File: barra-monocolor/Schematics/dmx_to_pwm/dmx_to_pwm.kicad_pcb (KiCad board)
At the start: 2 copper layers, 46 x 162.3 mm, 50 parts, among them J1 RJ45, J2 RJ45, J3 Conn_02x04_Top_Bottom, J5 Conn_01x05_Socket, Q1 TIP41, Q2 TIP41, Q3 TIP41, Q5 TIP41, SW1 SW_DIP_x08, U2 LM2596T-5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

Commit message: updated max patches
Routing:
- net 5V: track 224.1 -> 219.0 mm
- net Net-(D3-A): track 62.6 -> 62.1 mm

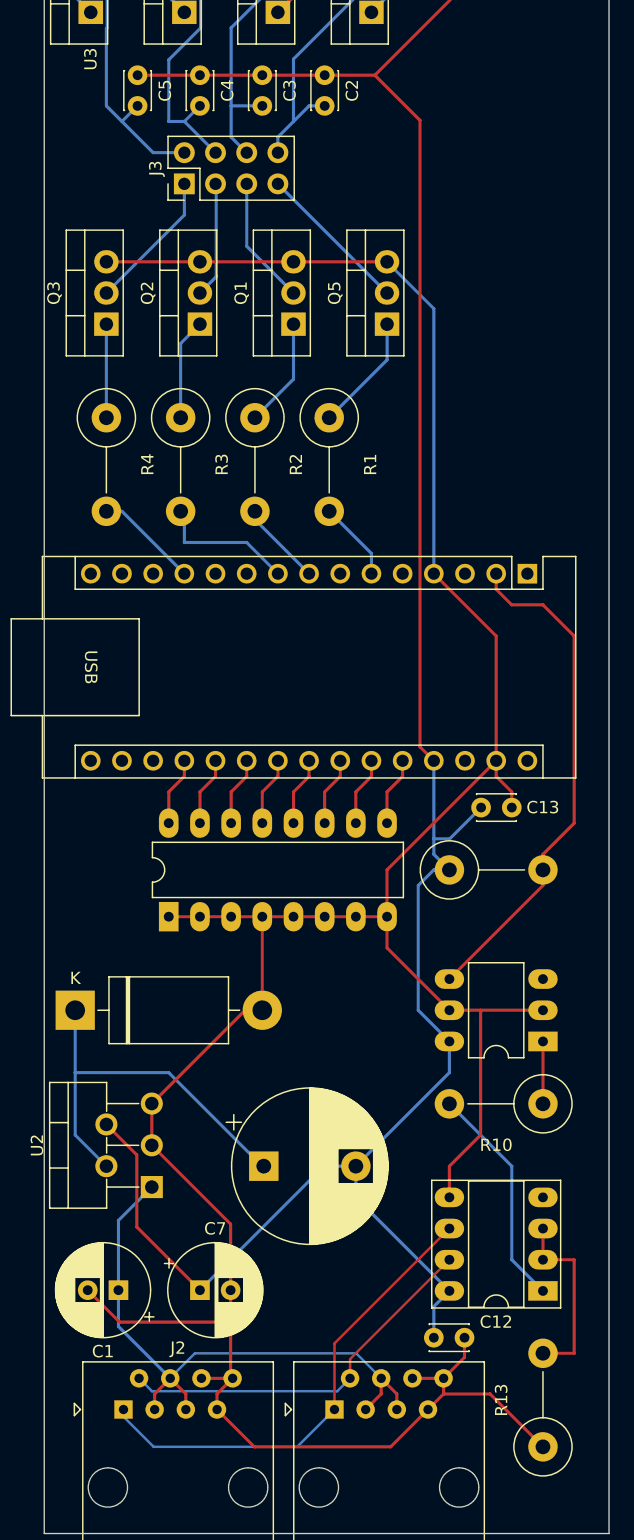
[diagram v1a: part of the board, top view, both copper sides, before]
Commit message: improved pcb track width, added antenna connector
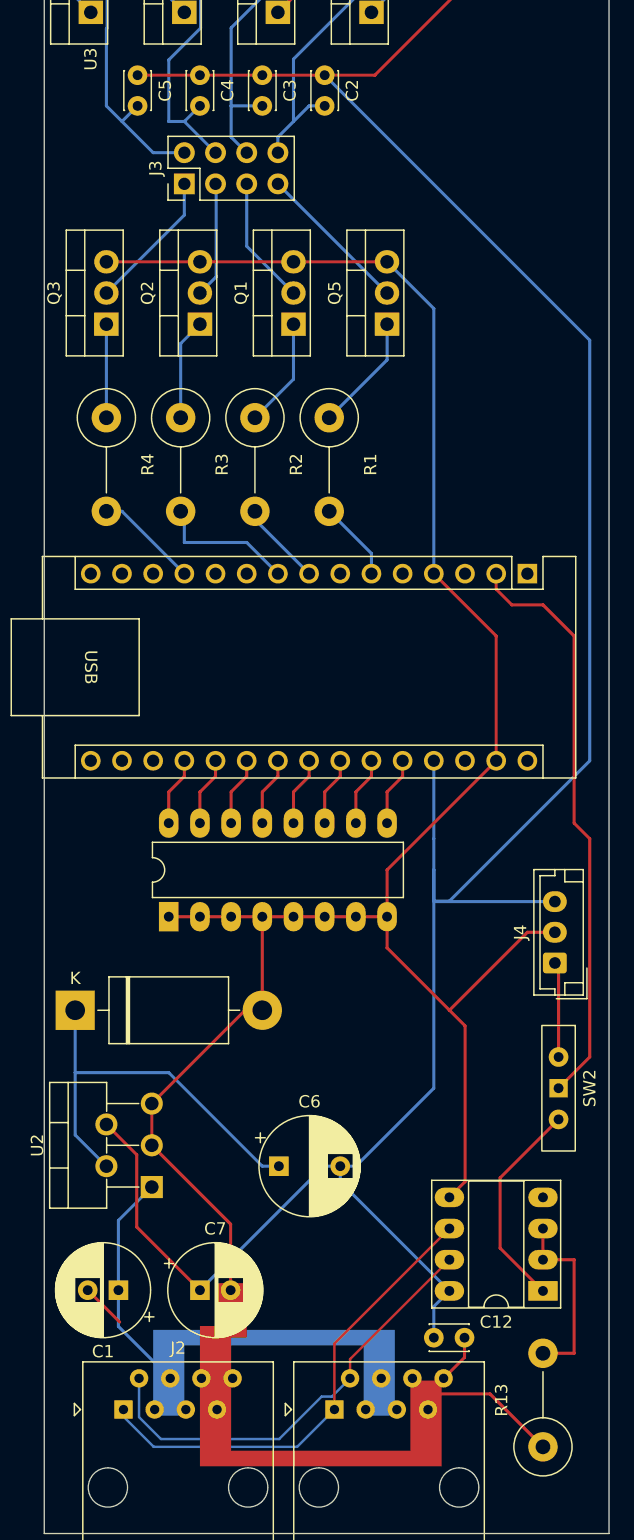
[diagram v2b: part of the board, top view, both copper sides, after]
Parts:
- removed C13: 100nF, Capacitor_THT:C_Disc_D3.0mm_W2.0mm_P2.50mm
- removed L1: 100uH, Capacitor_THT:CP_Radial_D12.5mm_P7.50mm
- removed R10: 470, Resistor_THT:R_Axial_DIN0414_L11.9mm_D4.5mm_P7.62mm_Vertical
- removed R14: 1K, Resistor_THT:R_Axial_DIN0414_L11.9mm_D4.5mm_P7.62mm_Vertical
- removed U9: H11L1, Package_DIP:DIP-6_W7.62mm_LongPads
- added C6: 33uH, Capacitor_THT:CP_Radial_D8.0mm_P5.00mm, F.Cu at (86.4, 154.9)
- added J4: Conn_01x03_Socket, Connector_JST:JST_EH_B3B-EH-A_1x03_P2.50mm_Vertical, F.Cu at (108.9, 138.4)
- added SW2: SW_Wuerth, Button_Switch_THT:SW_Slide-03_Wuerth-WS-SLTV_10x2.5x6.4_P2.54mm, F.Cu at (109.2, 148.6)
- C1: value 47uF - 50V -> 47uF - 100V
- C7: value 47uF - 50V -> 47uF - 16V
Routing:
- net GND: track 241.7 -> 203.6 mm
- net VCC: track 49.6 -> 18.5 mm
- net 5V: track 219.0 -> 247.5 mm
- net Net-(J4-Pin_1): track 0.00 -> 7.78 mm
- net Net-(A1-D0/RX): track 41.3 -> 47.6 mm
- net Net-(R10-Pad1): track 5.08 -> 0.00 mm
- net DATA-: track 31.1 -> 36.1 mm
- net Net-(D2-K): track 32.3 -> 33.5 mm
- net Net-(SW2-A): track 18.4 -> 17.4 mm

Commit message: stuff
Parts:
- removed D5: 1N4004, Diode_THT:D_DO-41_SOD81_P7.62mm_Horizontal
- removed U6: LM337_TO220, Package_TO_SOT_THT:TO-220-3_Vertical
- added D1: 1N4004, Diode_THT:D_DO-41_SOD81_P7.62mm_Horizontal, F.Cu at (96.5, 35.6)
- added H1: MountingHole_Pad, MountingHole:MountingHole_3.2mm_M3_Pad, F.Cu at (109.2, 47.6)
- added H2: MountingHole_Pad, MountingHole:MountingHole_3.2mm_M3_Pad, F.Cu at (71.8, 74.3)
- added H3: MountingHole_Pad, MountingHole:MountingHole_3.2mm_M3_Pad, F.Cu at (71.8, 130.8)
- added H4: MountingHole_Pad, MountingHole:MountingHole_3.2mm_M3_Pad, F.Cu at (96.5, 148.0)
- added H5: MountingHole_Pad, MountingHole:MountingHole_3.2mm_M3_Pad, F.Cu at (104.8, 94.0)
- added U1: LM317_TO-220, Package_TO_SOT_THT:TO-220-3_Vertical, F.Cu at (70.2, 56.5)
- U3, U4, U5: value LM337_TO220 -> LM317_TO-220
- moved D4 11.2 mm to (96.5, 51.4), turned to 0 degrees
- moved D3 10.8 mm to (96.5, 43.2), turned to 0 degrees
- moved U4 8.28 mm to (85.7, 56.5), turned to -90 degrees
- moved U3 7.75 mm to (77.5, 56.5), turned to -90 degrees
- moved D6 7.62 mm to (96.5, 27.9), turned to 0 degrees
- moved U5 4.45 mm to (94.0, 56.5), turned to -90 degrees
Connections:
- C10 pad 1: 5V -> GND
- C10 pad 2: Net-(D5-A) -> Net-(D1-K)
- C11 pad 1: 5V -> GND
- C11 pad 2: Net-(D6-A) -> Net-(D6-K)
- C2 pad 1: 5V -> GND
- C3 pad 1: 5V -> GND
- C4 pad 1: 5V -> GND
- C5 pad 1: 5V -> GND
- C8 pad 1: 5V -> GND
- C8 pad 2: Net-(D3-A) -> Net-(D4-K)
- C9 pad 1: 5V -> GND
- C9 pad 2: Net-(D4-A) -> Net-(D3-K)
- D3 pad 1: 5V -> Net-(D3-K)
- D3 pad 2: Net-(D3-A) -> GND
- D4 pad 1: 5V -> Net-(D4-K)
- D4 pad 2: Net-(D4-A) -> GND
- D6 pad 1: 5V -> Net-(D6-K)
- D6 pad 2: Net-(D6-A) -> GND
- J5 pad 1: Net-(D3-A) -> Net-(D4-K)
- J5 pad 2: Net-(D4-A) -> Net-(D3-K)
- J5 pad 3: 5V -> GND
- J5 pad 4: Net-(D5-A) -> Net-(D1-K)
- J5 pad 5: Net-(D6-A) -> Net-(D6-K)
- Q1 pad 2: L2-SOC-IN -> 5V
- Q1 pad 3: GND -> L2-SOC-IN
- Q2 pad 2: L3-SOC-IN -> 5V
- Q2 pad 3: GND -> L3-SOC-IN
- Q3 pad 2: L4-SOC-IN -> 5V
- Q3 pad 3: GND -> L4-SOC-IN
- Q5 pad 2: L1-SOC-IN -> 5V
- Q5 pad 3: GND -> L1-SOC-IN
- R7 pad 2: Net-(U6-VO) -> Net-(U4-VO)
- R8 pad 2: Net-(U4-VO) -> Net-(U3-VO)
- R9 pad 2: Net-(U3-VO) -> Net-(U1-VO)
- RV1 pad 3: Net-(D3-A) -> Net-(D4-K)
- RV2 pad 3: Net-(D4-A) -> Net-(D3-K)
- RV3 pad 3: Net-(D5-A) -> Net-(D1-K)
- RV4 pad 3: Net-(D6-A) -> Net-(D6-K)
- U3 pad 1: Net-(D6-A) -> Net-(D1-K)
- U3 pad 2: L4-SOC-OUT -> Net-(U3-VO)
- U3 pad 3: Net-(U3-VO) -> L3-SOC-OUT
- U4 pad 1: Net-(D5-A) -> Net-(D3-K)
- U4 pad 2: L3-SOC-OUT -> Net-(U4-VO)
- U4 pad 3: Net-(U4-VO) -> L2-SOC-OUT
- U5 pad 1: Net-(D3-A) -> Net-(D4-K)
- U5 pad 2: L1-SOC-OUT -> Net-(U5-VO)
- U5 pad 3: Net-(U5-VO) -> L1-SOC-OUT
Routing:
- net Net-(D6-A): track 80.6 -> 0.00 mm
- net GND: track 203.6 -> 283.9 mm
- net Net-(D6-K): track 0.00 -> 77.6 mm
- net Net-(D5-A): track 76.8 -> 0.00 mm
- net Net-(D4-A): track 73.5 -> 0.00 mm
- net Net-(D1-K): track 0.00 -> 73.3 mm
- net Net-(D3-K): track 0.00 -> 67.4 mm
- net Net-(D3-A): track 62.1 -> 0.00 mm
- net Net-(D4-K): track 0.00 -> 55.9 mm
- net 5V: track 247.5 -> 194.7 mm
- net VCC: track 18.5 -> 0.00 mm
- net Net-(U1-VO): track 0.00 -> 11.9 mm
- net Net-(U3-VO): track 5.08 -> 11.8 mm
- net Net-(U6-VO): track 6.13 -> 0.00 mm
- net L3-SOC-OUT: track 19.7 -> 14.9 mm
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
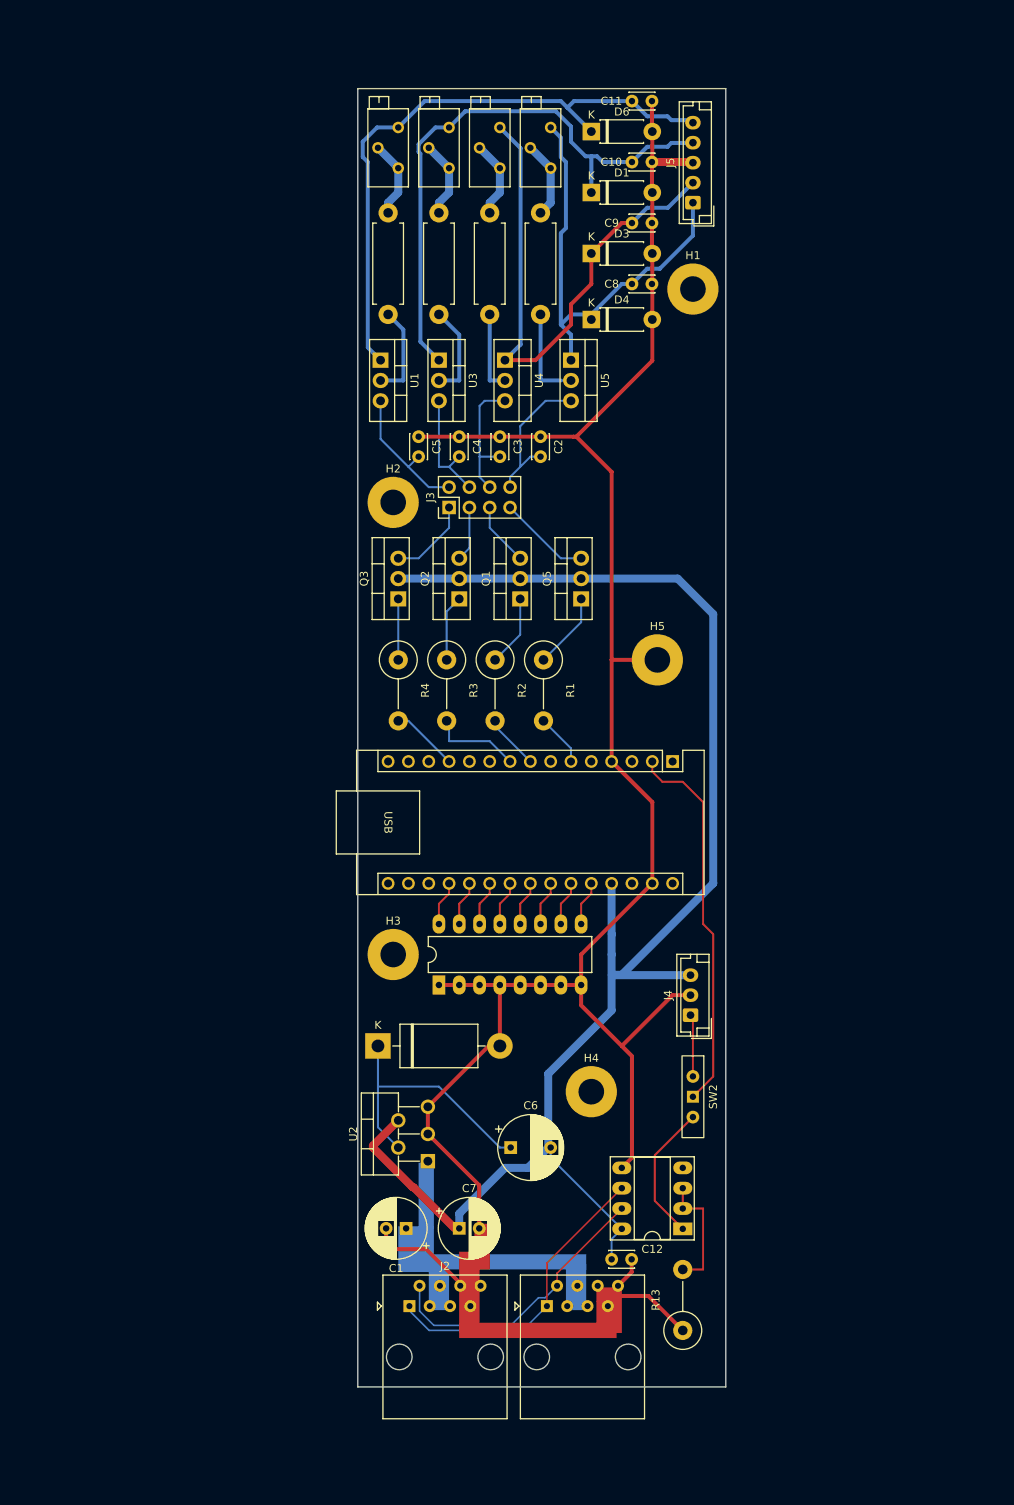
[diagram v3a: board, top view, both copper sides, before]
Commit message: updated schematics to 6 lasers
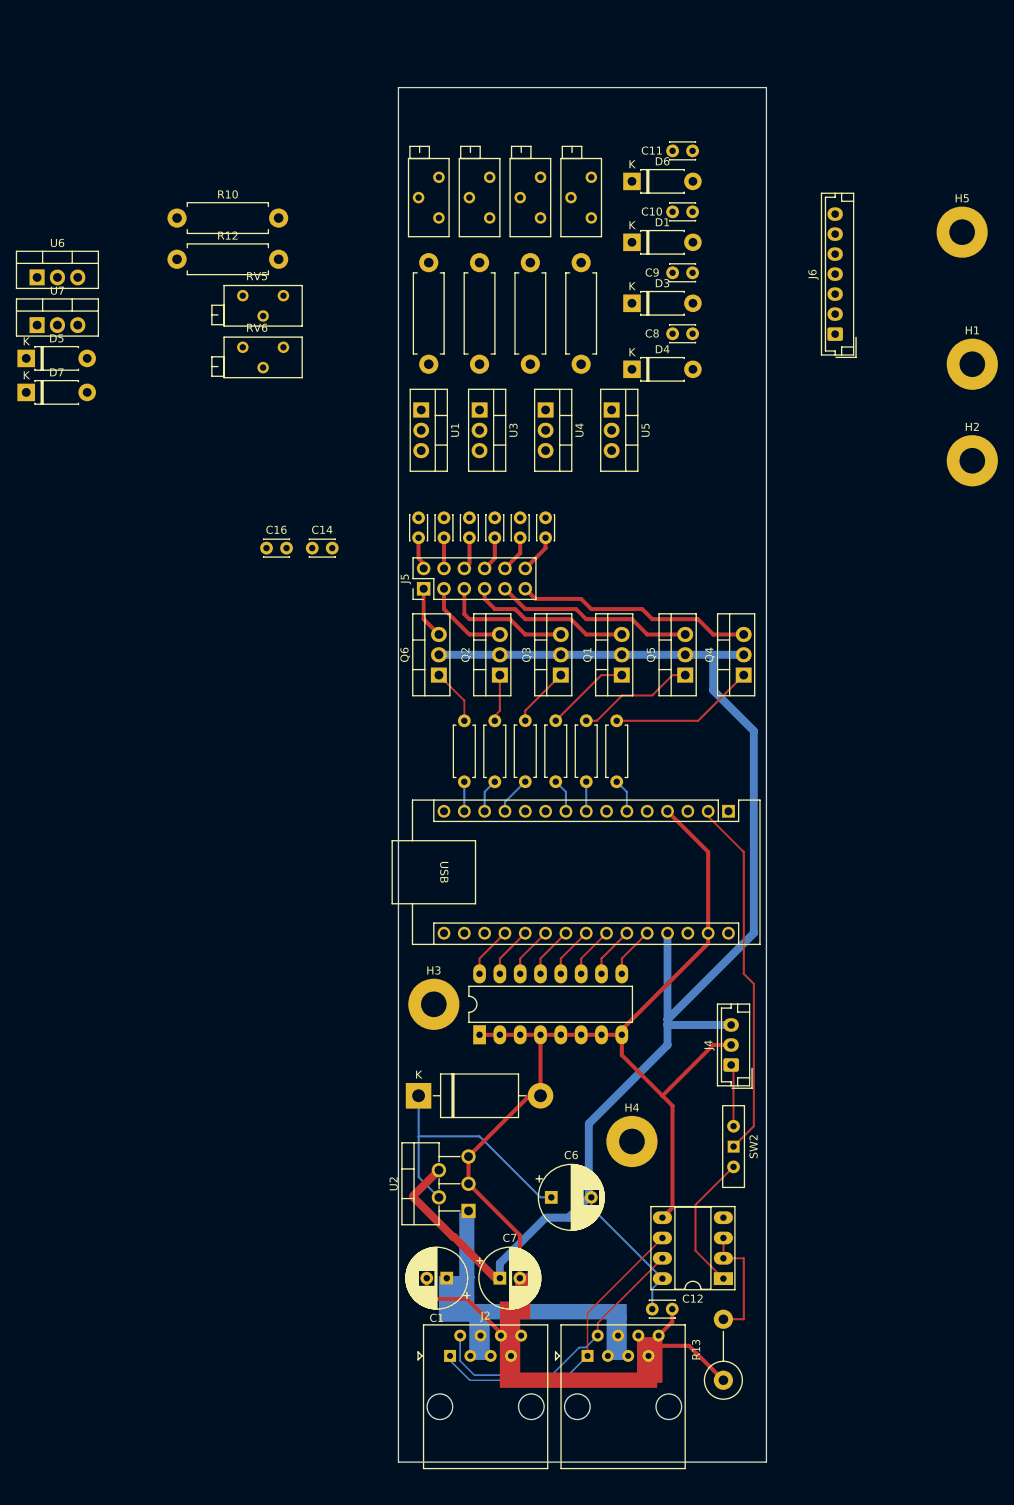
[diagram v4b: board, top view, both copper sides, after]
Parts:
- removed J3: Conn_02x04_Top_Bottom, Connector_PinHeader_2.54mm:PinHeader_2x04_P2.54mm_Vertical
- added C13: 100nF, Capacitor_THT:C_Disc_D3.0mm_W2.0mm_P2.50mm, F.Cu at (90.8, 76.2)
- added C14: 1uF, Capacitor_THT:C_Disc_D3.0mm_W2.0mm_P2.50mm, F.Cu at (61.6, 80.0)
- added C15: 100nF, Capacitor_THT:C_Disc_D3.0mm_W2.0mm_P2.50mm, F.Cu at (74.9, 76.2)
- added C16: 1uF, Capacitor_THT:C_Disc_D3.0mm_W2.0mm_P2.50mm, F.Cu at (55.9, 80.0)
- added D5: 1N4004, Diode_THT:D_DO-41_SOD81_P7.62mm_Horizontal, F.Cu at (25.9, 56.3)
- added D7: 1N4004, Diode_THT:D_DO-41_SOD81_P7.62mm_Horizontal, F.Cu at (25.9, 60.5)
- added J6: Conn_01x07_Socket, Connector_JST:JST_EH_B7B-EH-A_1x07_P2.50mm_Vertical, F.Cu at (127.0, 53.3)
- added Q4: TIP41, Package_TO_SOT_THT:TO-220-3_Vertical, F.Cu at (115.6, 95.9)
- added Q6: TIP41, Package_TO_SOT_THT:TO-220-3_Vertical, F.Cu at (77.5, 95.9)
- added R10: 2.7, Resistor_THT:R_Axial_DIN0411_L9.9mm_D3.6mm_P12.70mm_Horizontal, F.Cu at (44.7, 38.8)
- added R11: 1K, Resistor_THT:R_Axial_DIN0207_L6.3mm_D2.5mm_P7.62mm_Horizontal, F.Cu at (80.6, 101.6)
- added R12: 2.7, Resistor_THT:R_Axial_DIN0411_L9.9mm_D3.6mm_P12.70mm_Horizontal, F.Cu at (44.7, 43.9)
- added R5: 1K, Resistor_THT:R_Axial_DIN0207_L6.3mm_D2.5mm_P7.62mm_Horizontal, F.Cu at (99.7, 101.6)
- added RV5: 20, Potentiometer_THT:Potentiometer_Bourns_3296Z_Horizontal, F.Cu at (58.0, 48.5)
- added RV6: 20, Potentiometer_THT:Potentiometer_Bourns_3296Z_Horizontal, F.Cu at (58.0, 54.9)
- added U6: LM317_TO-220, Package_TO_SOT_THT:TO-220-3_Vertical, F.Cu at (27.2, 46.2)
- added U7: LM317_TO-220, Package_TO_SOT_THT:TO-220-3_Vertical, F.Cu at (27.2, 52.1)
- J5: value Conn_01x05_Socket -> Conn_02x06_Counter_Clockwise; footprint Connector_JST:JST_EH_B5B-EH-A_1x05_P2.50mm_Vertical -> Connector_PinHeader_2.54mm:PinHeader_2x06_P2.54mm_Vertical
- R1, R2, R3, R4: footprint Resistor_THT:R_Axial_DIN0414_L11.9mm_D4.5mm_P7.62mm_Vertical -> Resistor_THT:R_Axial_DIN0207_L6.3mm_D2.5mm_P7.62mm_Horizontal
- moved H2 72.6 mm to (144.1, 69.1)
- moved H5 65.7 mm to (142.9, 40.5)
- moved J5 58.8 mm to (75.6, 85.1)
- moved H1 36.2 mm to (144.1, 57.0)
- moved Q3 22.4 mm to (92.7, 95.9)
- moved R4 17.6 mm to (88.3, 101.6)
- moved Q5 16.1 mm to (108.3, 95.9)
- moved Q1 15.9 mm to (100.3, 95.9)
- moved Q2 10.8 mm to (85.1, 95.9)
- moved R2 10.7 mm to (92.1, 101.6)
- moved C5 10.6 mm to (78.1, 76.2)
- moved C2 10.5 mm to (87.6, 76.2)
- moved C4 10.2 mm to (81.3, 76.2)
- moved C3 10.2 mm to (84.5, 76.2)
- moved R3 9.71 mm to (84.5, 101.6)
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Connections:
- A1 pad 13: unconnected-(A1-D10-Pad13) -> LASER5
- A1 pad 14: unconnected-(A1-D11-Pad14) -> LASER6
- C2 pad 2: L1-SOC-OUT -> L2-SOC-OUT
- C3 pad 2: L2-SOC-OUT -> L3-SOC-OUT
- C4 pad 2: L3-SOC-OUT -> L4-SOC-OUT
- C5 pad 2: L4-SOC-OUT -> L5-SOC-OUT
- J5 pad 1: Net-(D4-K) -> L6-SOC-IN
- J5 pad 2: Net-(D3-K) -> L6-SOC-OUT
- J5 pad 3: GND -> L5-SOC-IN
- J5 pad 4: Net-(D1-K) -> L5-SOC-OUT
- J5 pad 5: Net-(D6-K) -> L4-SOC-IN
- Q1 pad 3: L2-SOC-IN -> L3-SOC-IN
- Q2 pad 3: L3-SOC-IN -> L5-SOC-IN
- Q5 pad 3: L1-SOC-IN -> L2-SOC-IN
- R1 pad 2: LASER1 -> LASER2
- R2 pad 2: LASER2 -> LASER3
- R3 pad 2: LASER3 -> LASER5
- U1 pad 3: L4-SOC-OUT -> L5-SOC-OUT
- U3 pad 3: L3-SOC-OUT -> L4-SOC-OUT
- U4 pad 3: L2-SOC-OUT -> L3-SOC-OUT
- U5 pad 3: L1-SOC-OUT -> L2-SOC-OUT
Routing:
- net GND: track 283.9 -> 166.0 mm
- net Net-(D6-K): track 77.6 -> 0.00 mm
- net Net-(D1-K): track 73.3 -> 0.00 mm
- net Net-(D3-K): track 67.4 -> 0.00 mm
- net Net-(D4-K): track 55.9 -> 0.00 mm
- net Net-(Q4-B): track 0.00 -> 18.2 mm
- net L1-SOC-IN: track 11.5 -> 29.7 mm
- net L2-SOC-IN: track 7.93 -> 24.9 mm
- net L1-SOC-OUT: track 18.9 -> 4.88 mm
- net L4-SOC-OUT: track 17.6 -> 4.09 mm
- net L3-SOC-IN: track 6.95 -> 20.3 mm
- net Net-(U5-VO): track 12.1 -> 0.00 mm
- net L2-SOC-OUT: track 16.7 -> 4.62 mm
- net Net-(U1-VO): track 11.9 -> 0.00 mm
- net Net-(U3-VO): track 11.8 -> 0.00 mm
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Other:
- board size 46 x 162.3 mm -> 46 x 171.8 mm
